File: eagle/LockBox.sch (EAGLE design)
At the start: 18 parts

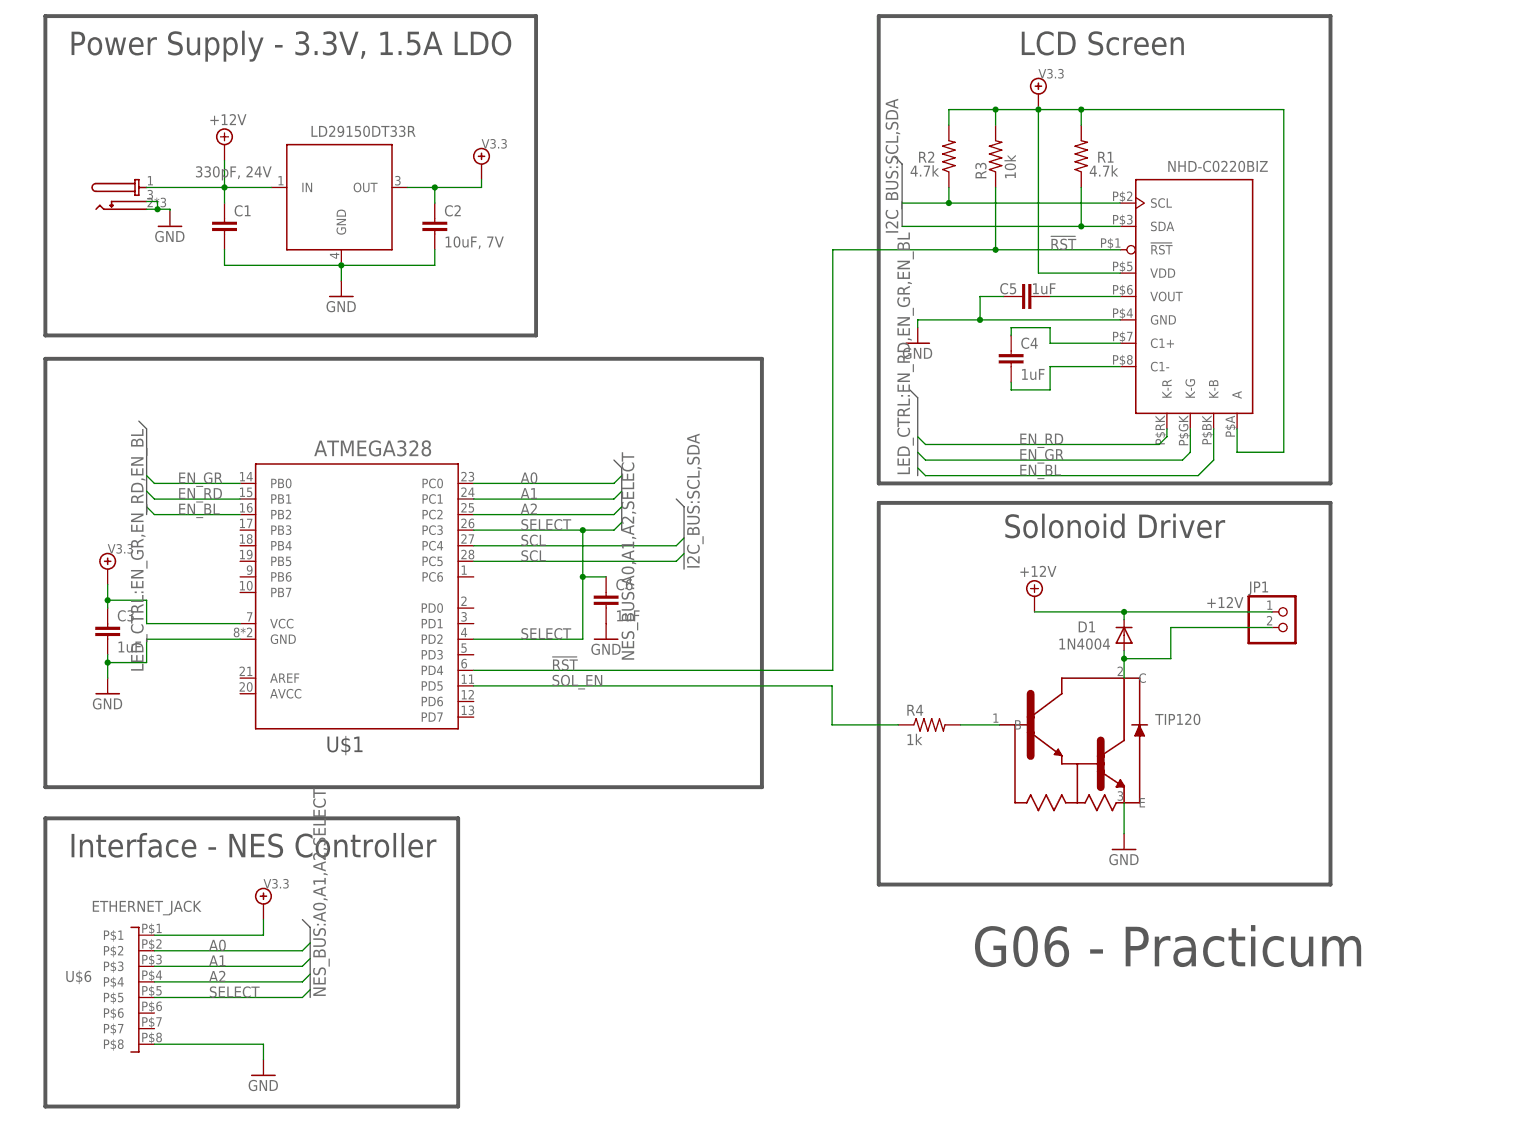
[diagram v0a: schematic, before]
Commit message: Added AVCC connection to VCC on the ATMEL chip. Added document number.
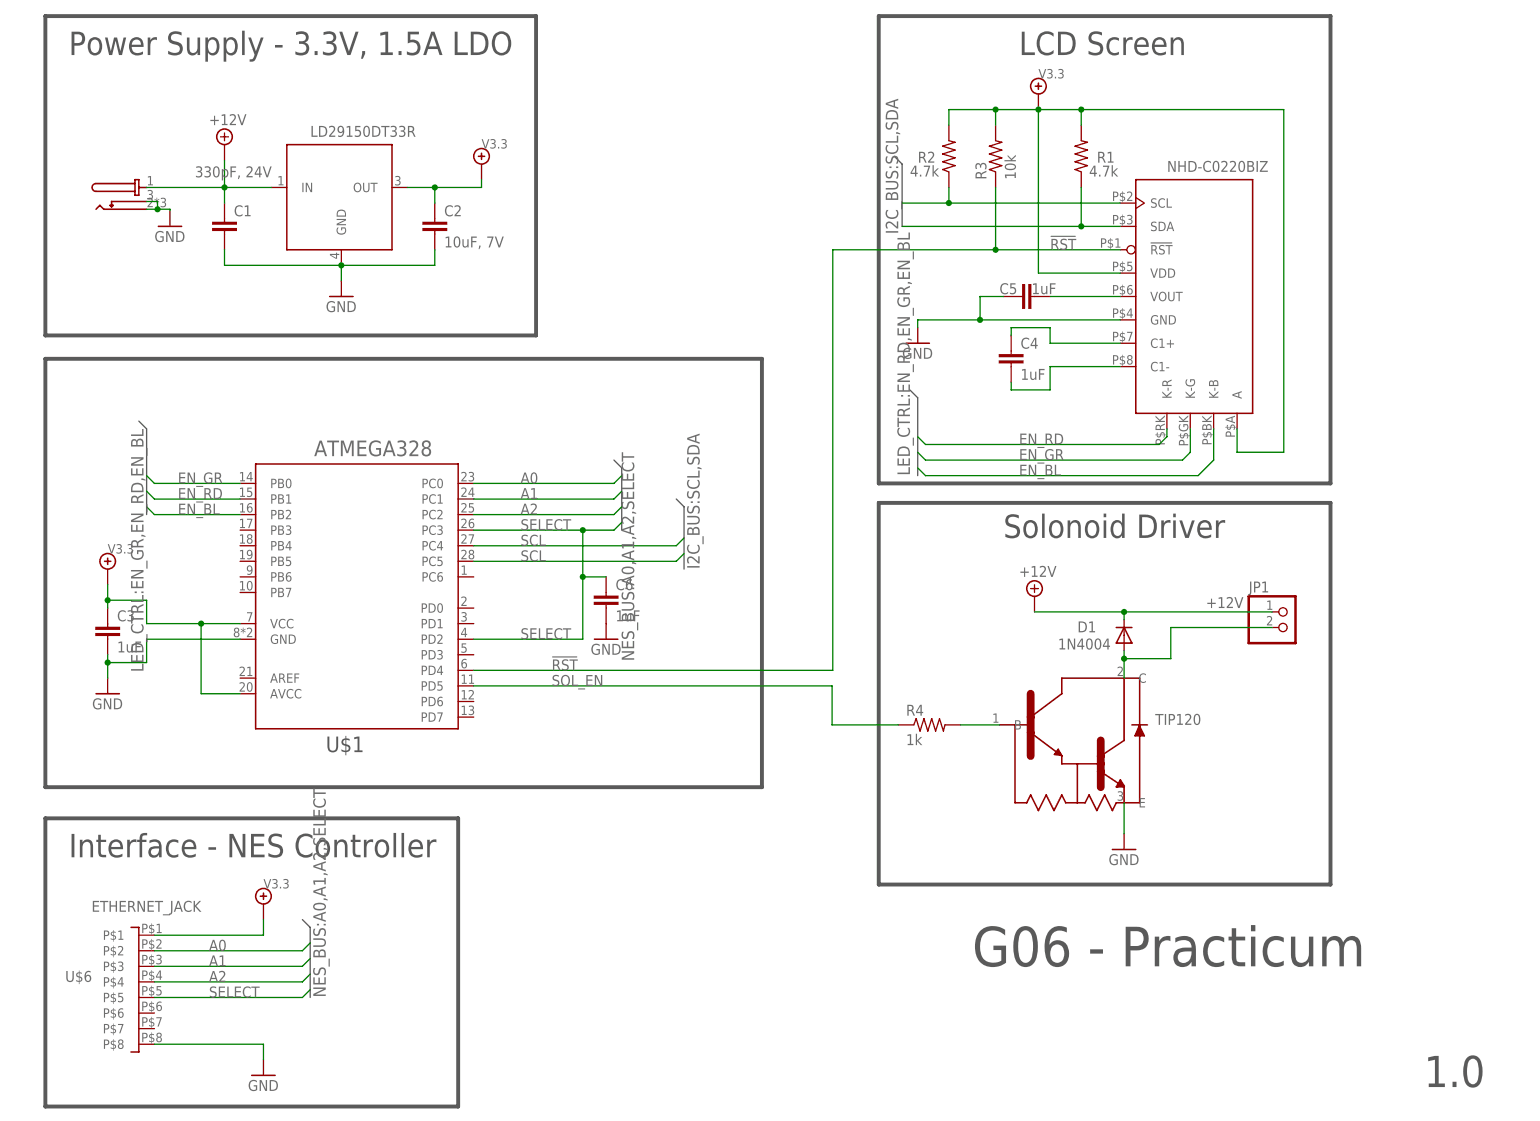
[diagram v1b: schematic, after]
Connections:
- removed net P$1: C2.1, C3.1, R1.2, R2.2, R3.2, U$1.VCC, U$2.OUT, U$5.A, U$5.VDD, U$6.P$1
- new net 3.3V: C2.1, C3.1, R1.2, R2.2, R3.2, U$1.AVCC, U$1.VCC, U$2.OUT, U$5.A, U$5.VDD, U$6.P$1
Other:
- note added: "1.0"
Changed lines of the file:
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@@
 <?xml version="1.0" encoding="utf-8"?>
 <!DOCTYPE eagle SYSTEM "eagle.dtd">
-<eagle version="6.6.0">
+<eagle version="7.1.0">
 <drawing>
 <settings>
@@
 <setting verticaltext="up"/>
 </settings>
-<grid distance="0.05" unitdist="inch" unit="inch" style="lines" multiple="1" display="yes" altdistance="0.01" altunitdist="inch" altunit="inch"/>
+<grid distance="0.025" unitdist="inch" unit="inch" style="lines" multiple="1" display="yes" altdistance="0.01" altunitdist="inch" altunit="inch"/>
 <layers>
 <layer number="1" name="Top" color="4" fill="1" visible="no" active="no"/>
@@
 <text x="167.64" y="95.25" size="3.81" layer="97">Solonoid Driver</text>
 <text x="162.56" y="25.4" size="6.4516" layer="97">G06 - Practicum</text>
+<text x="236.22" y="5.715" size="5.08" layer="97">1.0</text>
 </plain>
 <instances>
@@
 </segment>
 </net>
-<net name="P$1" class="0">
+<net name="3.3V" class="0">
 <segment>
 <pinref part="U$2" gate="G$1" pin="OUT"/>
@@
 <segment>
 <pinref part="U$1" gate="G$1" pin="VCC"/>
-<wire x1="43.18" y1="81.28" x2="27.94" y2="81.28" width="0.1524" layer="91"/>
+<wire x1="43.18" y1="81.28" x2="36.83" y2="81.28" width="0.1524" layer="91"/>
+<wire x1="36.83" y1="81.28" x2="27.94" y2="81.28" width="0.1524" layer="91"/>
 <wire x1="27.94" y1="81.28" x2="27.94" y2="85.09" width="0.1524" layer="91"/>
 <wire x1="27.94" y1="85.09" x2="21.59" y2="85.09" width="0.1524" layer="91"/>
@@
 <wire x1="21.59" y1="85.09" x2="21.59" y2="87.63" width="0.1524" layer="91"/>
 <junction x="21.59" y="85.09"/>
-</segment>
-<segment>
+<pinref part="U$1" gate="G$1" pin="AVCC"/>
+<wire x1="43.18" y1="69.85" x2="36.83" y2="69.85" width="0.1524" layer="91"/>
+<wire x1="36.83" y1="69.85" x2="36.83" y2="81.28" width="0.1524" layer="91"/>
+<junction x="36.83" y="81.28"/>
+</segment>
+<segment>

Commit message: Added 6pin 2x3 headder to the Lockbox.sch.  Routed necessary nets associated with programing the ATMEL chip.  A switch will need to be added for the RESET. This schematic version is 1.1.
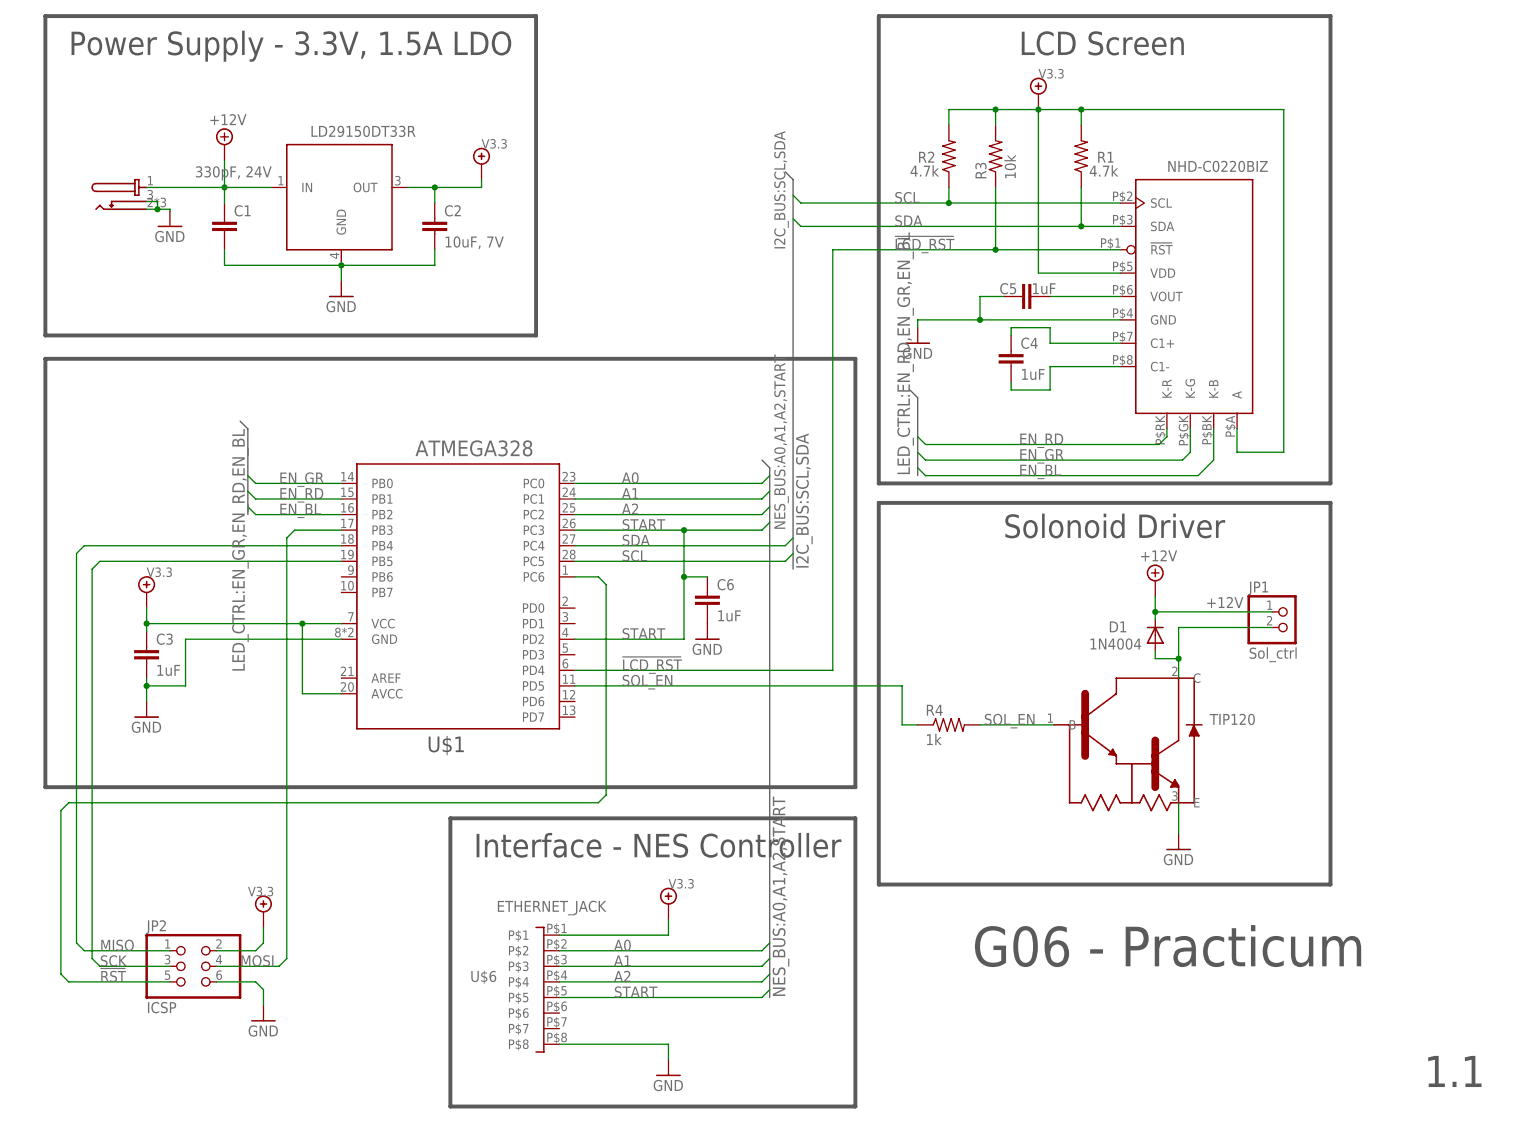
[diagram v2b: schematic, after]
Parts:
- added JP2: ICSP, LockBox:PINHD-2X3
- JP1: value (none) -> Sol_ctrl
- U$1: PB3 (none) -> MOSI; PB4 (none) -> MISO; PB5 (none) -> SCK; PC6 (none) -> RESET
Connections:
- net SELECT renamed START
- new net !LCD_RST: R3.1, U$1.PD4, U$5.!RST
- new net MISO: JP2.1, U$1.PB4
- new net MOSI: JP2.4, U$1.PB3
- new net SCK: JP2.3, U$1.PB5
- net !RST: now also JP2.5, U$1.PC6; no longer R3.1, U$1.PD4, U$5.!RST
- net 3.3V: now also JP2.2
- net GND: now also JP2.6
- net SCL: no longer U$1.PC4
- net SDA: now also U$1.PC4
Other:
- note added: "1.1"
- note removed: "1.0"
- moved on the sheet: C3, C6, D1, R4, U$1, U$6

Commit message: Moved EN_RD from PB1 to PB0 and EN_GR from PB0 to PB1, this change was necessary to aid in board layout
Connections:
- net EN_GR: now also U$1.PB1; no longer U$1.PB0
- net EN_RD: now also U$1.PB0; no longer U$1.PB1
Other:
- note added: "T06 - Practicum"
- note removed: "G06 - Practicum"
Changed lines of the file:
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@@
 <wire x1="220.98" y1="38.735" x2="220.98" y2="100.965" width="0.635" layer="97"/>
 <text x="167.64" y="95.25" size="3.81" layer="97">Solonoid Driver</text>
-<text x="162.56" y="25.4" size="6.4516" layer="97">G06 - Practicum</text>
+<text x="162.56" y="25.4" size="6.4516" layer="97">T06 - Practicum</text>
 <text x="236.22" y="5.715" size="5.08" layer="97">1.1</text>
 </plain>
@@
 <net name="EN_GR" class="0">
 <segment>
-<wire x1="44.45" y1="105.41" x2="45.72" y2="104.14" width="0.1524" layer="91"/>
-<pinref part="U$1" gate="G$1" pin="PB0"/>
-<wire x1="45.72" y1="104.14" x2="59.69" y2="104.14" width="0.1524" layer="91"/>
-<label x="49.53" y="104.14" size="1.778" layer="95"/>
-</segment>
-<segment>
 <pinref part="U$5" gate="G$1" pin="K-G"/>
 <wire x1="198.12" y1="113.03" x2="198.12" y2="109.22" width="0.1524" layer="91"/>
@@
 <label x="170.18" y="107.95" size="1.778" layer="95"/>
 </segment>
-</net>
-<net name="EN_RD" class="0">
 <segment>
 <wire x1="44.45" y1="102.87" x2="45.72" y2="101.6" width="0.1524" layer="91"/>
@@
 <label x="49.53" y="101.6" size="1.778" layer="95"/>
 </segment>
+</net>
+<net name="EN_RD" class="0">
 <segment>
 <pinref part="U$5" gate="G$1" pin="K-R"/>
@@
 <label x="170.18" y="110.49" size="1.778" layer="95"/>
 </segment>
-</net>
+<segment>
+<wire x1="44.45" y1="105.41" x2="45.72" y2="104.14" width="0.1524" layer="91"/>
+<pinref part="U$1" gate="G$1" pin="PB0"/>
+<wire x1="45.72" y1="104.14" x2="59.69" y2="104.14" width="0.1524" layer="91"/>
+<label x="49.53" y="104.14" size="1.778" layer="95"/>
+</segment>
+</net>

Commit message: Finished first draft of board layout. I have not ran a DRU yet because I dont have the OSHPARK DRU files.
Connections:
- new net N$1: R4.2, U$4.B
- net SOL_EN: no longer R4.2, U$4.B
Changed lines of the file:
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@@
 <net name="SOL_EN" class="0">
 <segment>
-<pinref part="U$4" gate="GATE" pin="B"/>
-<pinref part="R4" gate="G$1" pin="2"/>
-<wire x1="175.895" y1="64.77" x2="163.83" y2="64.77" width="0.1524" layer="91"/>
-<label x="164.465" y="64.77" size="1.778" layer="95"/>
-</segment>
-<segment>
-<pinref part="R4" gate="G$1" pin="1"/>
 <pinref part="U$1" gate="G$1" pin="PD5"/>
-<wire x1="153.67" y1="64.77" x2="151.13" y2="64.77" width="0.1524" layer="91"/>
 <wire x1="151.13" y1="64.77" x2="151.13" y2="71.12" width="0.1524" layer="91"/>
 <wire x1="151.13" y1="71.12" x2="97.79" y2="71.12" width="0.1524" layer="91"/>
 <label x="105.41" y="71.12" size="1.778" layer="95"/>
+<pinref part="R4" gate="G$1" pin="1"/>
+<wire x1="151.13" y1="64.77" x2="153.67" y2="64.77" width="0.1524" layer="91"/>
 </segment>
 </net>
@@
 </segment>
 </net>
+<net name="N$1" class="0">
+<segment>
+<pinref part="R4" gate="G$1" pin="2"/>
+<pinref part="U$4" gate="GATE" pin="B"/>
+<wire x1="163.83" y1="64.77" x2="175.895" y2="64.77" width="0.1524" layer="91"/>
+</segment>
+</net>
